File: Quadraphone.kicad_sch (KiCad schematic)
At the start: 32 parts, among them J1 Eurorack_10_pin_power, SW1 SYNCH_SWITCH, SW2 DPDT_Switch, U1 AMS1117-5.0, U10 TL074, U14 TL074, U19 TL074, U2 MCP1501-25xSN, U4 LM4040DBZ-5, U5 MCP6004, U8 4066

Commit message: Started PCB layout
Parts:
- removed PWM_Pot1, Vibrato_Depth1: 10k, Custom_Footprints:Alpha_9mm_Potentiometer_Aligned, symbol Device:R_Potentiometer_Small
- removed SW1: SYNCH_SWITCH, symbol Switch:SW_SPDT
- removed SW2: DPDT_Switch, symbol Custom_Audio:DPDT_Switch
- gave numbers to parts that had none: 4
- renumbered J1 to J5
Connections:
- net PWM_CV: now reaches J4.8 (Pin_8)
- net HARD_SYNCH_SW_IN renamed HARD_SYNCH_SW
- net PULSE_SW_IN renamed PULSE_SW
- net SAW_SW_IN renamed SAW_SW
- net SOFT_SYNCH_SW_IN renamed SOFT_SYNCH_SW
- net TRI_SW_IN renamed TRIANGLE_SW
- no-connect marks 0 -> 2
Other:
- sheet OSCVoice1 ports: added PWM_CV_ALL; removed none
- sheet OSCVoice2 ports: added PWM_CV_ALL; removed none
- sheet OSCVoice3 ports: added PWM_CV_ALL; removed none
- sheet OSCVoice4 ports: added PWM_CV_ALL; removed none
- moved on the sheet: J1, R1, R10, R2, R3, R6

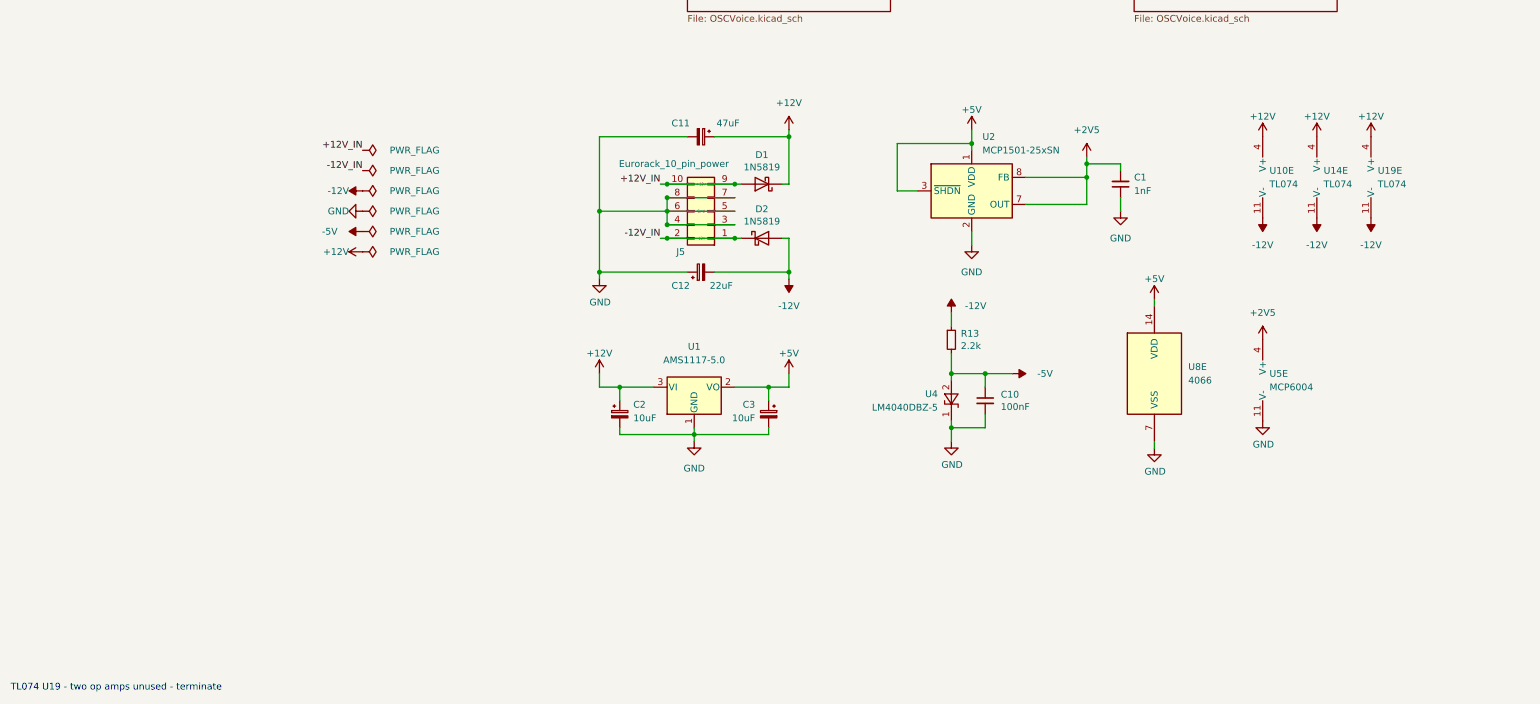
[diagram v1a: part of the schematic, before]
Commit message: Updated design to use buffered 2.5V reference
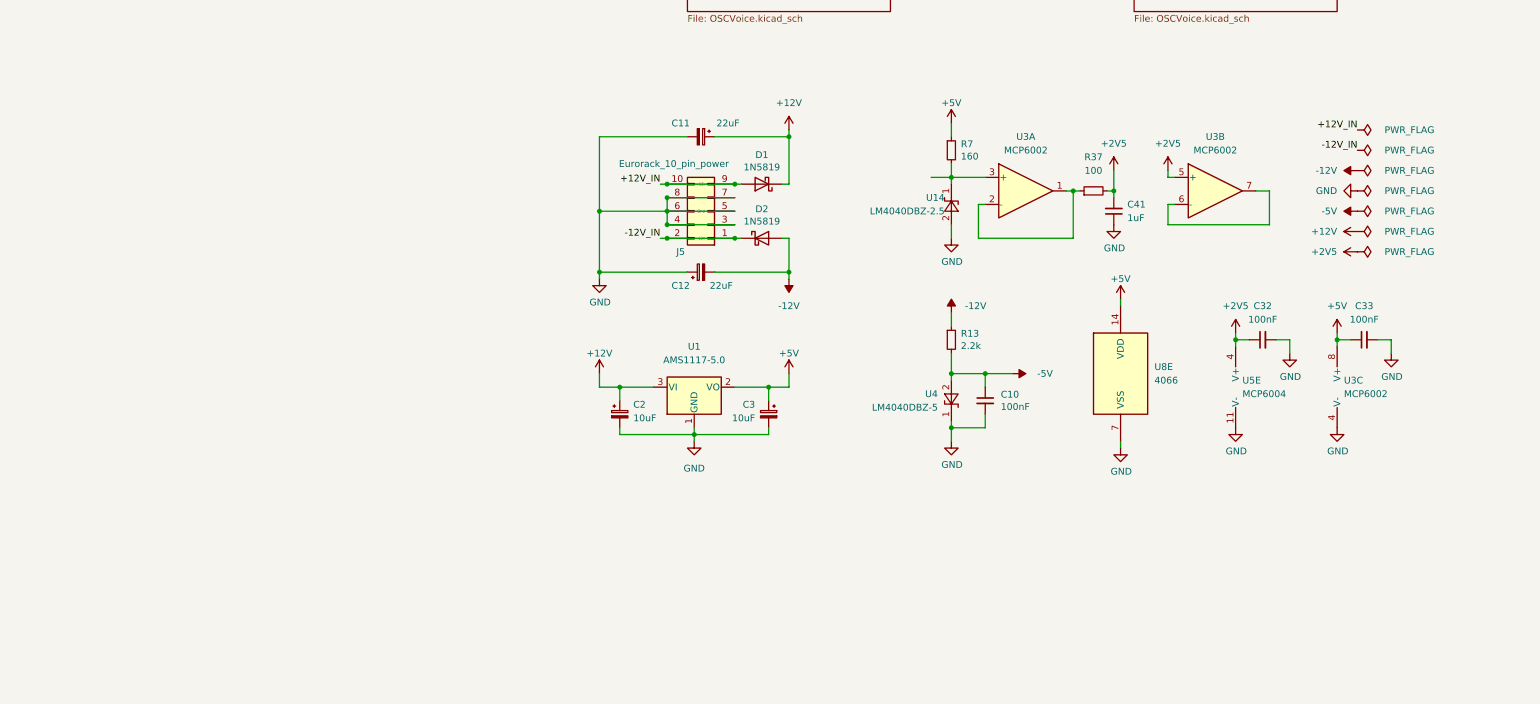
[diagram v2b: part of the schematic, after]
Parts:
- removed C1: 1nF, Capacitor_SMD:C_0603_1608Metric_Pad1.08x0.95mm_HandSolder, symbol Device:C_Small
- removed U10, U14, U19: TL074, Package_SO:SOIC-14_3.9x8.7mm_P1.27mm, symbol Amplifier_Operational:TL074
- removed U2: MCP1501-25xSN, Package_SO:SOIC-8_3.9x4.9mm_P1.27mm, symbol Reference_Voltage:MCP1501-25xSN
- added C32, C33: 100nF, Capacitor_SMD:C_0603_1608Metric_Pad1.08x0.95mm_HandSolder, symbol Device:C_Small
- added C41: 1uF, Capacitor_SMD:C_0603_1608Metric_Pad1.08x0.95mm_HandSolder, symbol Device:C_Small
- added R37: 100, Resistor_SMD:R_0603_1608Metric, symbol Device:R_Small
- added R7: 160, Resistor_SMD:R_0805_2012Metric, symbol Device:R_Small
- added U14: LM4040DBZ-2.5, Package_TO_SOT_SMD:SOT-23, symbol Reference_Voltage:LM4040DBZ-2.5
- added U3: MCP6002, Package_SO:MSOP-8_3x3mm_P0.65mm, symbol Amplifier_Operational:MCP6002-xSN
- C11: value 47uF -> 22uF; footprint Capacitor_SMD:CP_Elec_5x5.8 -> Capacitor_SMD:CP_Elec_4x5.8
- C2, C3: footprint Capacitor_SMD:CP_Elec_5x5.7 -> Capacitor_SMD:CP_Elec_4x5.7
- C9: footprint Capacitor_SMD:C_0805_2012Metric -> Capacitor_SMD:C_0603_1608Metric_Pad1.08x0.95mm_HandSolder
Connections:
- net +2V5: now also C32.1, C41.2, R37.2, U3.5 (+)
- net +5V: now also C33.1, R7.1, U3.8 (V+)
- net GND: now also C32.2, C33.2, C41.1, U14.2 (A), U3.4 (V-)
- new net: U3.6 (-), U3.7
- new net: R37.1, U3.1, U3.2 (-)
- new net: R7.2, U14.1 (K), U3.3 (+)
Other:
- note removed: "TL074 U19 - two op amps unused - terminate"
- moved on the sheet: U5E, U8E

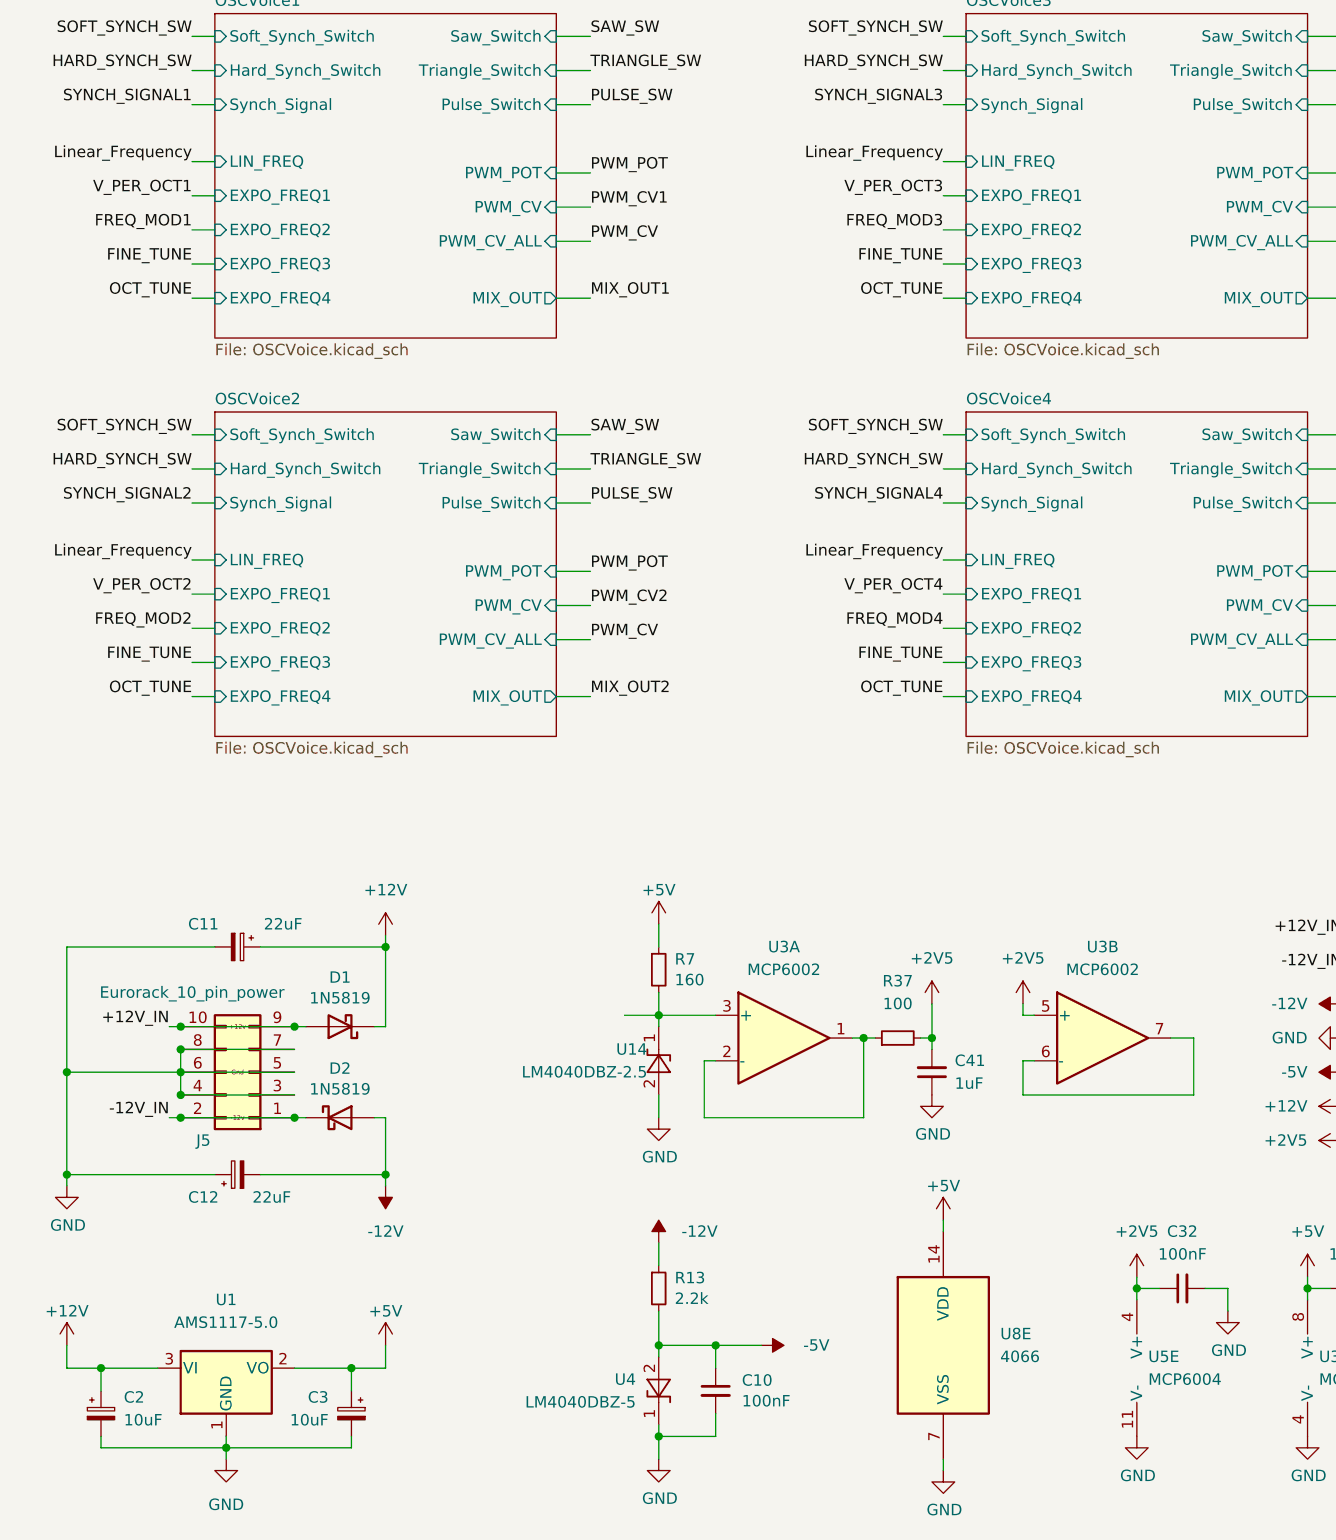
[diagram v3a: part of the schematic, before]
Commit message: Duplicated layout of voices; power supply
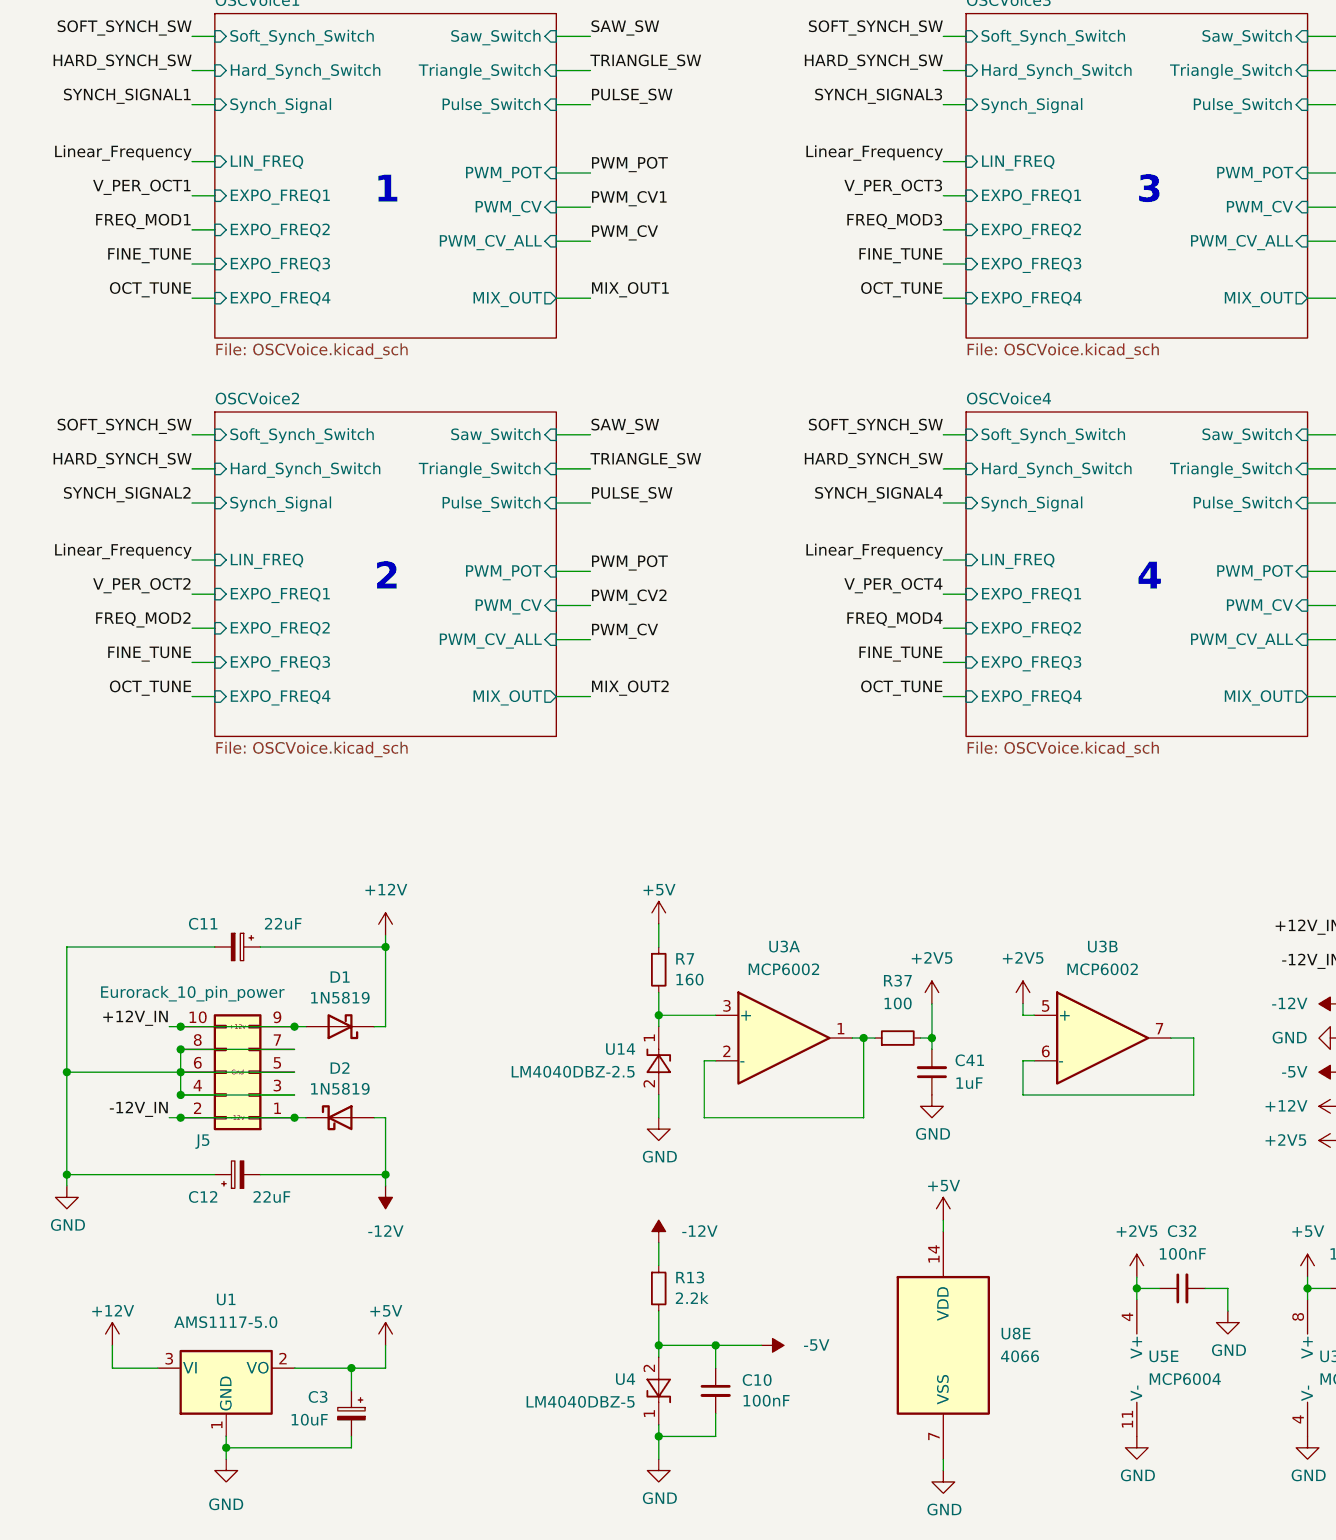
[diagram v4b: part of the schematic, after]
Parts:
- removed C2: 10uF, Capacitor_SMD:CP_Elec_4x5.7, symbol Device:C_Polarized_Small
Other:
- note added: "1"
- note added: "2"
- note added: "3"
- note added: "4"

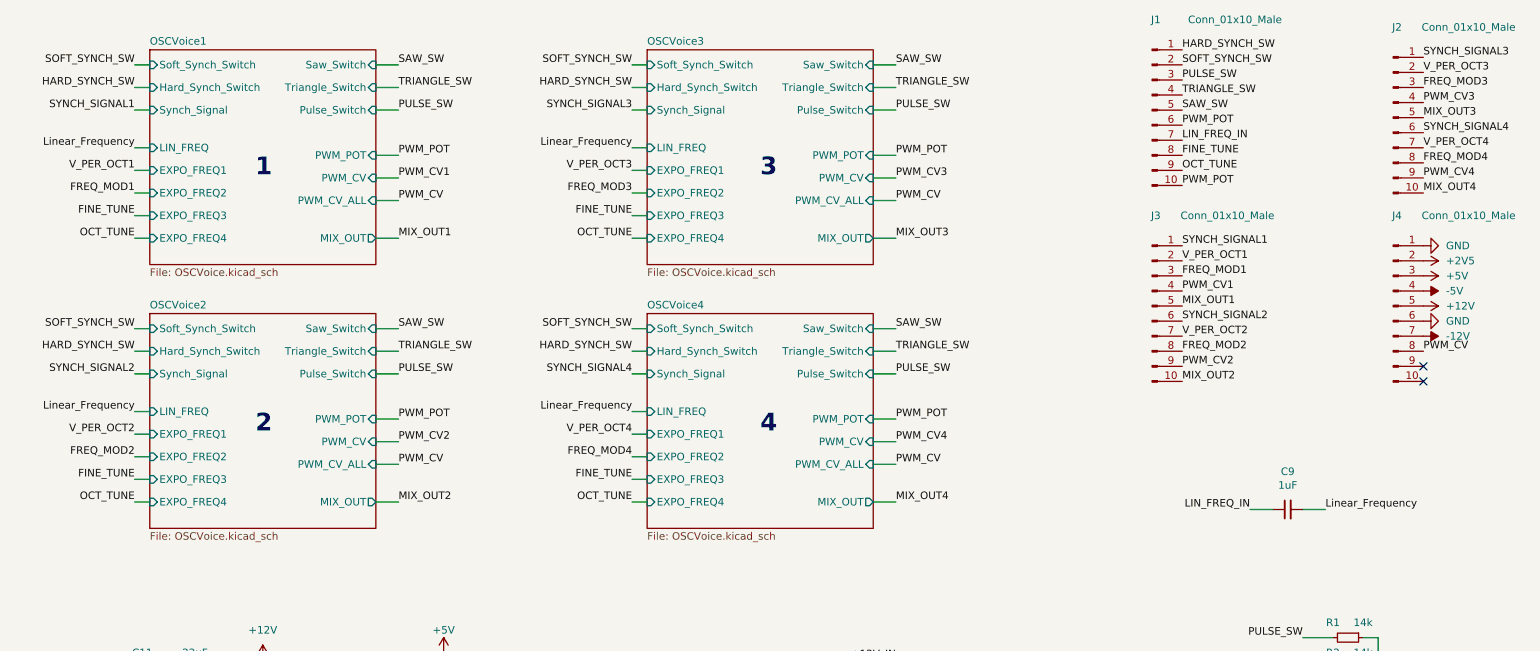
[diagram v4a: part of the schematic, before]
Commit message: Routed majority of signal traces
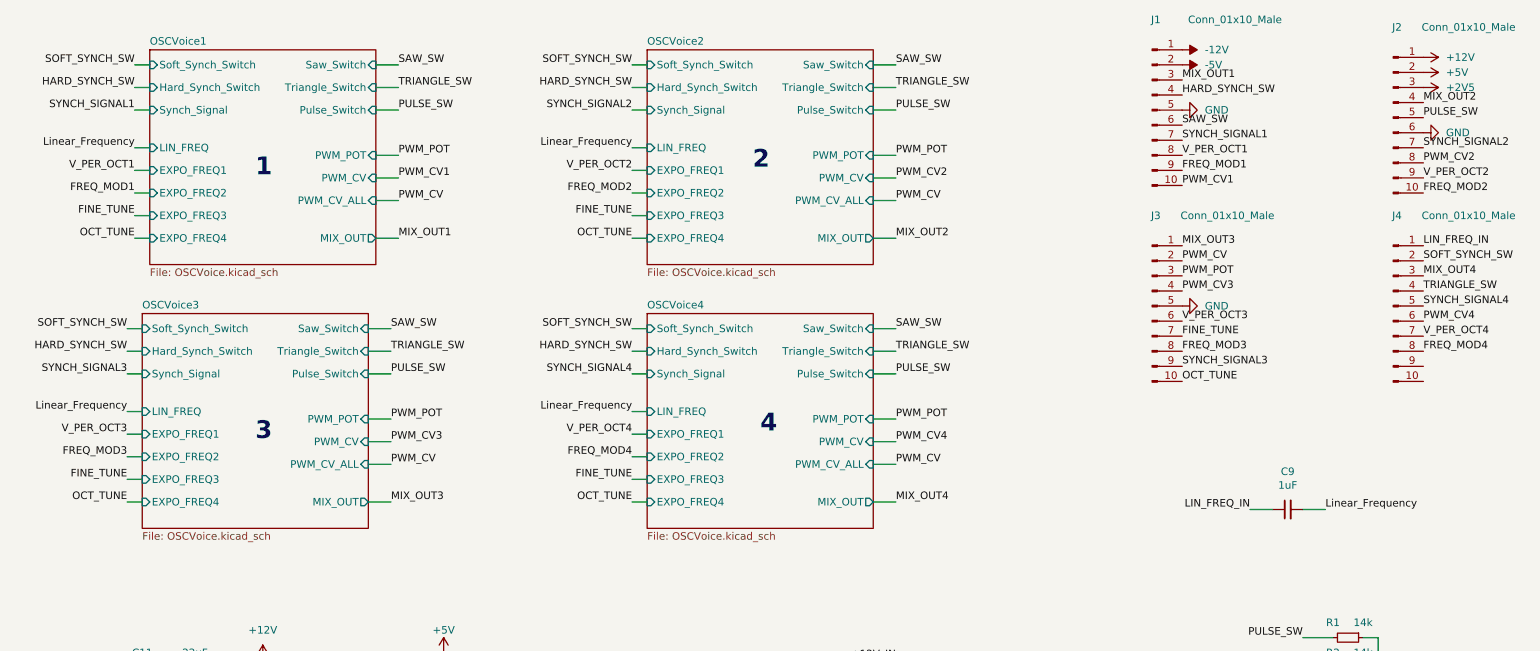
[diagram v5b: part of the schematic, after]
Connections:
- net +12V: now also J2.1 (Pin_1); no longer J4.5 (Pin_5)
- net +2V5: now also J2.3 (Pin_3); no longer J4.2 (Pin_2)
- net +5V: now also J2.2 (Pin_2); no longer J4.3 (Pin_3)
- net -12V: now also J1.1 (Pin_1); no longer J4.7 (Pin_7)
- net -5V: now also J1.2 (Pin_2); no longer J4.4 (Pin_4)
- net FINE_TUNE: now also J3.7 (Pin_7); no longer J1.8 (Pin_8)
- net FREQ_MOD1: now also J1.9 (Pin_9); no longer J3.3 (Pin_3)
- net FREQ_MOD2: now also J2.10 (Pin_10); no longer J3.8 (Pin_8)
- net FREQ_MOD3: now also J3.8 (Pin_8); no longer J2.3 (Pin_3)
- net FREQ_MOD4: now also J4.8 (Pin_8); no longer J2.8 (Pin_8)
- net GND: now also J1.5 (Pin_5), J2.6 (Pin_6), J3.5 (Pin_5); no longer J4.1 (Pin_1), J4.6 (Pin_6)
- net HARD_SYNCH_SW: now also J1.4 (Pin_4); no longer J1.1 (Pin_1)
- net LIN_FREQ_IN: now also J4.1 (Pin_1); no longer J1.7 (Pin_7)
- net MIX_OUT1: now also J1.3 (Pin_3); no longer J3.5 (Pin_5)
- net MIX_OUT2: now also J2.4 (Pin_4); no longer J3.10 (Pin_10)
- net MIX_OUT3: now also J3.1 (Pin_1); no longer J2.5 (Pin_5)
- net MIX_OUT4: now also J4.3 (Pin_3); no longer J2.10 (Pin_10)
- net OCT_TUNE: now also J3.10 (Pin_10); no longer J1.9 (Pin_9)
- net PULSE_SW: now also J2.5 (Pin_5); no longer J1.3 (Pin_3)
- net PWM_CV: now also J3.2 (Pin_2); no longer J4.8 (Pin_8)
- net PWM_CV1: now also J1.10 (Pin_10); no longer J3.4 (Pin_4)
- net PWM_CV2: now also J2.8 (Pin_8); no longer J3.9 (Pin_9)
- net PWM_CV3: now also J3.4 (Pin_4); no longer J2.4 (Pin_4)
- net PWM_CV4: now also J4.6 (Pin_6); no longer J2.9 (Pin_9)
- net PWM_POT: now also J3.3 (Pin_3); no longer J1.10 (Pin_10), J1.6 (Pin_6)
- net SAW_SW: now also J1.6 (Pin_6); no longer J1.5 (Pin_5)
- net SOFT_SYNCH_SW: now also J4.2 (Pin_2); no longer J1.2 (Pin_2)
- net SYNCH_SIGNAL1: now also J1.7 (Pin_7); no longer J3.1 (Pin_1)
- net SYNCH_SIGNAL2: now also J2.7 (Pin_7); no longer J3.6 (Pin_6)
- net SYNCH_SIGNAL3: now also J3.9 (Pin_9); no longer J2.1 (Pin_1)
- net SYNCH_SIGNAL4: now also J4.5 (Pin_5); no longer J2.6 (Pin_6)
- net TRIANGLE_SW: now also J4.4 (Pin_4); no longer J1.4 (Pin_4)
- net V_PER_OCT1: now also J1.8 (Pin_8); no longer J3.2 (Pin_2)
- net V_PER_OCT2: now also J2.9 (Pin_9); no longer J3.7 (Pin_7)
- net V_PER_OCT3: now also J3.6 (Pin_6); no longer J2.2 (Pin_2)
- net V_PER_OCT4: now also J4.7 (Pin_7); no longer J2.7 (Pin_7)
- no-connect marks 2 -> 0
